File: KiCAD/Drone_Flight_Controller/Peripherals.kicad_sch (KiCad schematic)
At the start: 39 parts, among them J2 Conn_01x03, J3 Conn_01x03, J301 XT60, J302 Conn_01x04, J4 Conn_01x03, J5 Conn_01x03, J6 USB_C_Receptacle_USB2.0_14P, Q501 2N2222A, U3 74AHC1G125, U4 74AHC1G125, U5 74AHC1G125, U6 74AHC1G125

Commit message: Re-annotate
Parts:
- +5V1: renamed from VBUS1; value VBUS -> +5V
- renumbered 3V3 to 3V1, BZ501 to BZ1, C302 to C1, D315 to D1, D4 to D3, D301 to D4, D302 to D5, D3 to D6, D5 to D7, F4 to F3, F3 to F4, J302 to GPS1, J301 to J1, J4 to Motor1, J5 to Motor2, J2 to Motor3, J3 to Motor4, Q501 to Q1, R8 to R1, R1 to R2, R501 to R3, R502 to R4, R303 to R5, R304 to R6, U5 to U1, U6 to U2, J6 to USB-C1

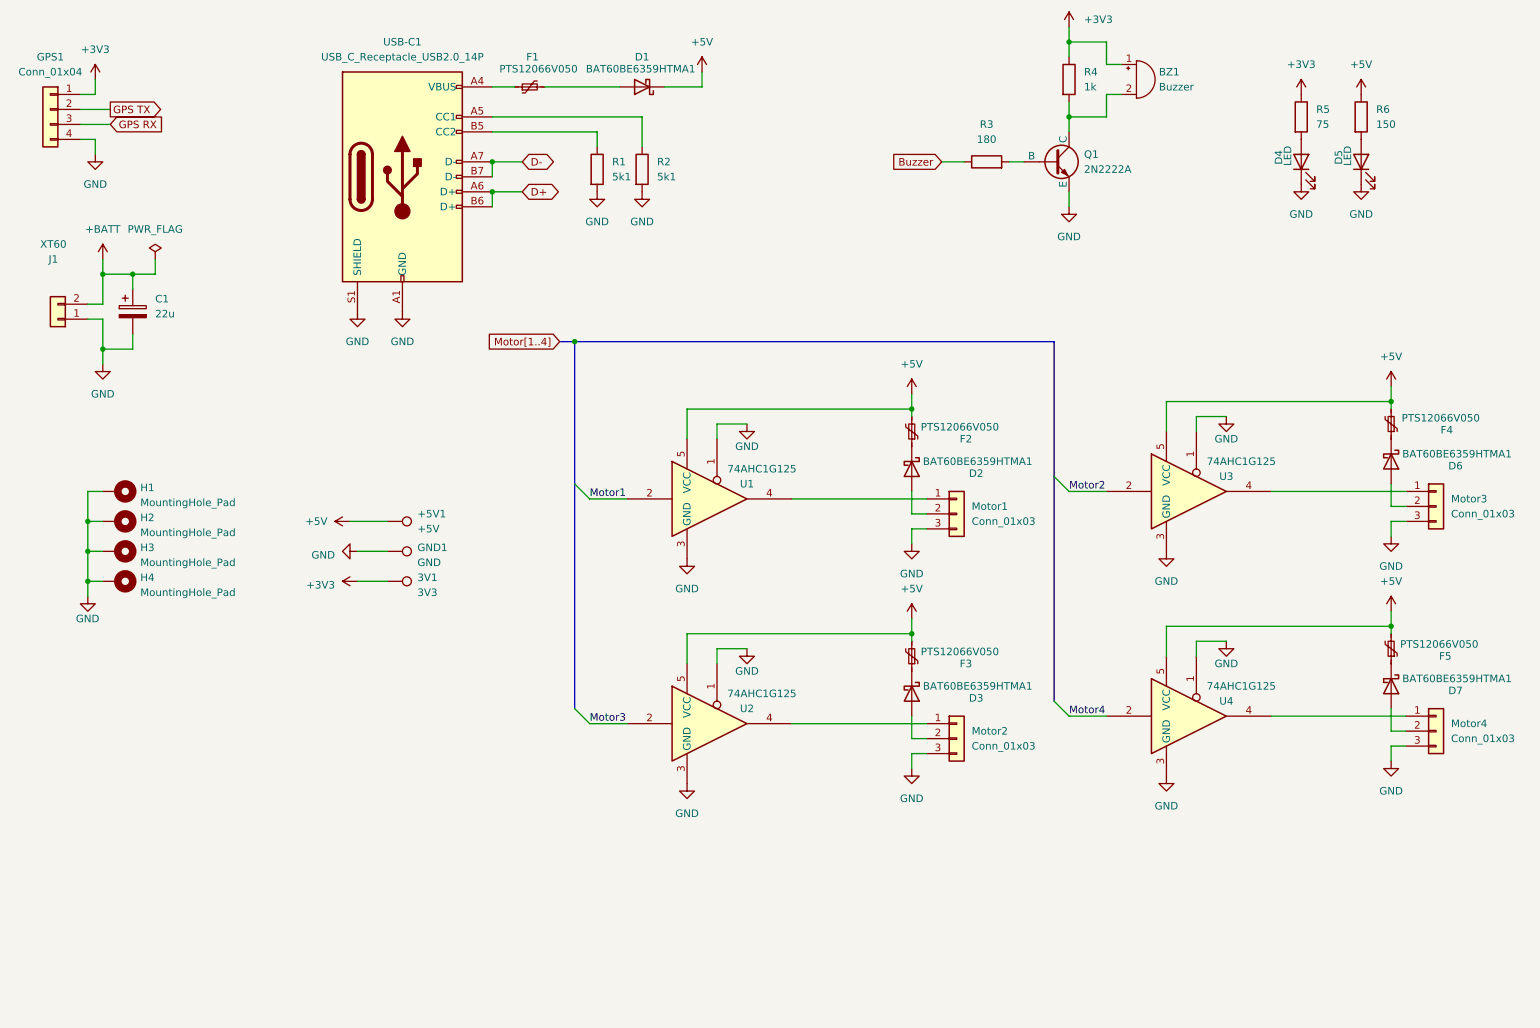
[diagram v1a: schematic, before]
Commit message: Add Status LEDs
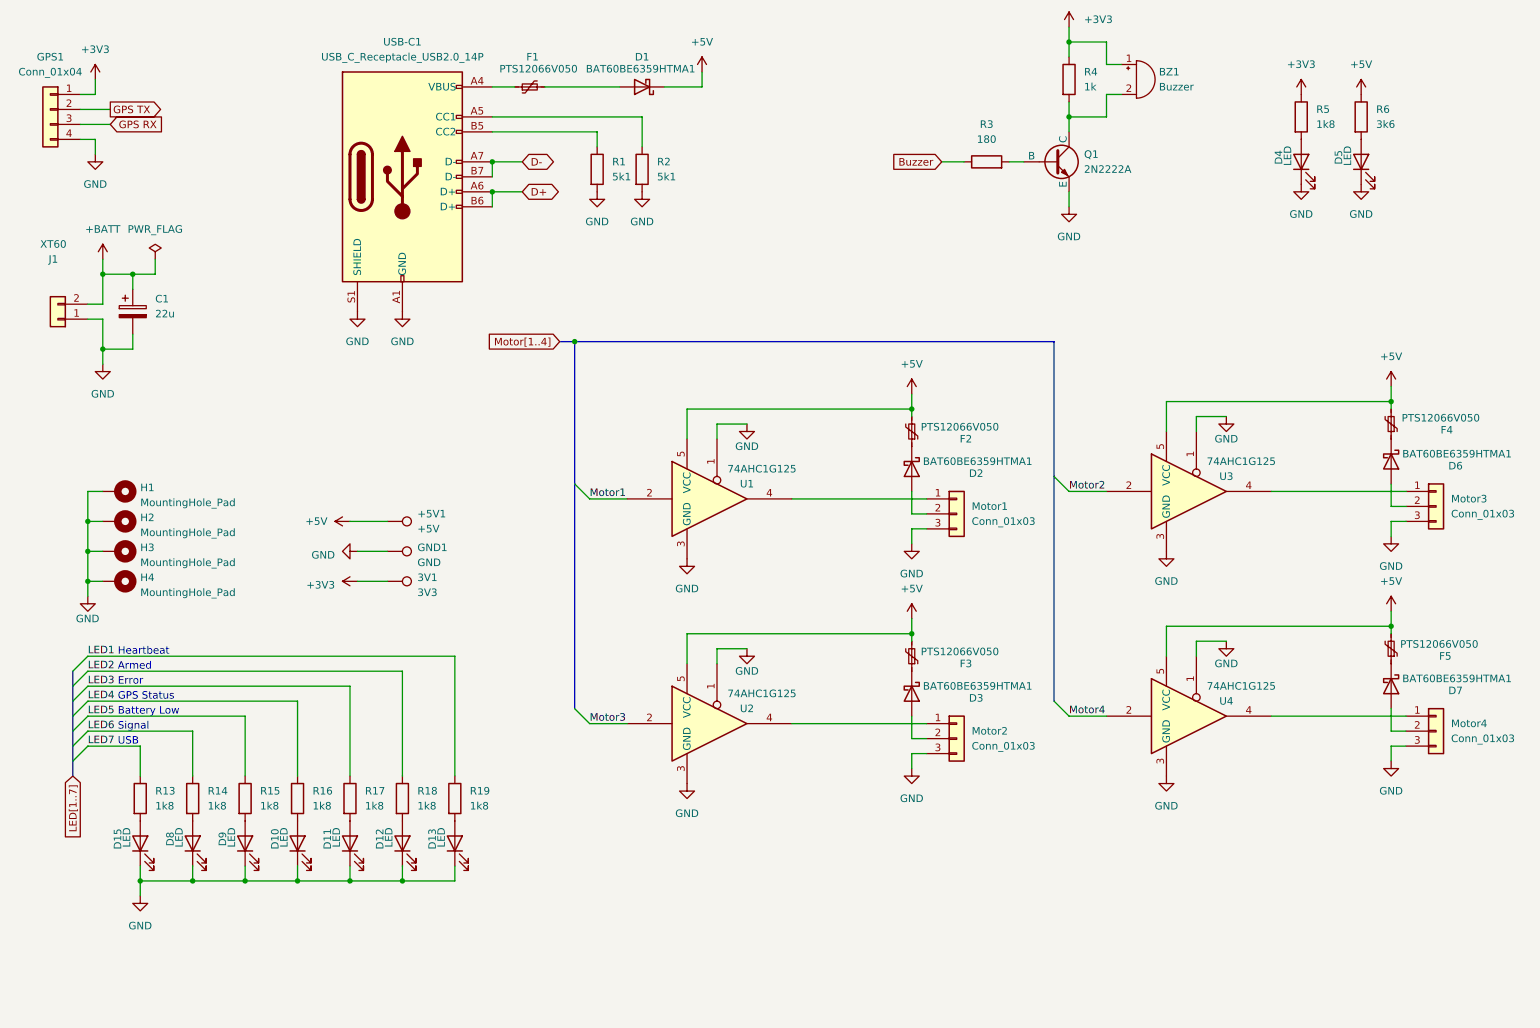
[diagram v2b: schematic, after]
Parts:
- added D10, D11, D12, D13, D15, D8, D9: LED, LED_SMD:LED_0805_2012Metric_Pad1.15x1.40mm_HandSolder, symbol Device:LED
- added R13, R14, R15, R16, R17, R18, R19: 1k8, symbol Device:R
- R5: value 75 -> 1k8; footprint Resistor_SMD:R_0805_2012Metric_Pad1.20x1.40mm_HandSolder -> (none); Link https://eu.mouser.com/ProductDetail/YAGEO/RC0805FR-0775RP?q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 -> (none)
- R6: value 150 -> 3k6
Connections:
- net GND: now also D10.1 (K), D11.1 (K), D12.1 (K), D13.1 (K), D15.1 (K), D8.1 (K), D9.1 (K)
- new net: D12.2 (A), R18.2
- new net: D15.2 (A), R13.2
- new net: D8.2 (A), R14.2
- new net: D11.2 (A), R17.2
- new net: D9.2 (A), R15.2
- new net: D13.2 (A), R19.2
- new net: D10.2 (A), R16.2
- new net LED1: R19.1
- new net LED2: R18.1
- new net LED3: R17.1
- new net LED4: R16.1
- new net LED5: R15.1
- new net LED6: R14.1
- new net LED7: R13.1
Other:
- note added: "Armed"
- note added: "Battery Low"
- note added: "Error"
- note added: "GPS Status"
- note added: "Heartbeat"
- note added: "Signal"
- note added: "USB"

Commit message: Fix Error with Motors
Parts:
- renumbered Motor3 to Motor2, Motor2 to Motor3
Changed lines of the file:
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@@
 		(dnp no)
 		(fields_autoplaced yes)
-		(property "Reference" "Motor3"
+		(property "Reference" "Motor2"
 			(at 269.24 107.9499 0)
 			(effects
@@
 			(project "Drone_Flight_Controller"
 				(path "/51ab9491-7068-4b24-bb38-47a0c739796e/a1832adb-c070-4778-a5ef-97ea378c06da"
-					(reference "Motor3")
+					(reference "Motor2")
 					(unit 1)
 				)
@@
 		(dnp no)
 		(fields_autoplaced yes)
-		(property "Reference" "Motor2"
+		(property "Reference" "Motor3"
 			(at 187.96 147.3199 0)
 			(effects
@@
 			(project "Drone_Flight_Controller"
 				(path "/51ab9491-7068-4b24-bb38-47a0c739796e/a1832adb-c070-4778-a5ef-97ea378c06da"
-					(reference "Motor2")
-					(unit 1)
-				)
+					(reference "Motor3")
+					(unit 1)
+				)

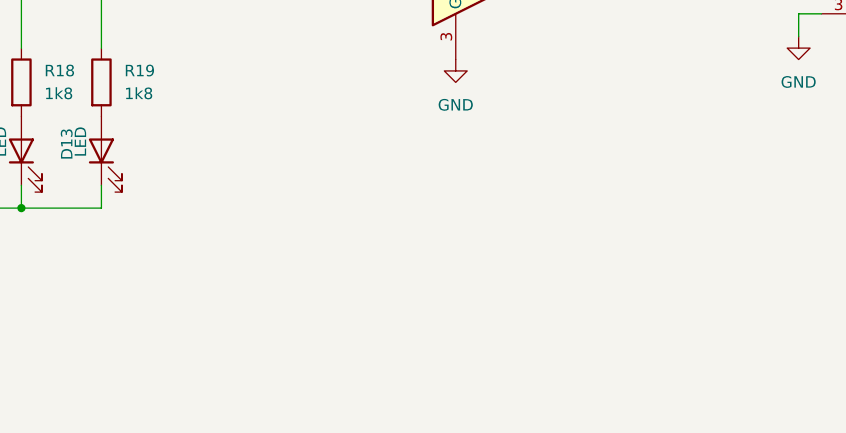
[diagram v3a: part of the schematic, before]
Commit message: Add Current and ESC sense
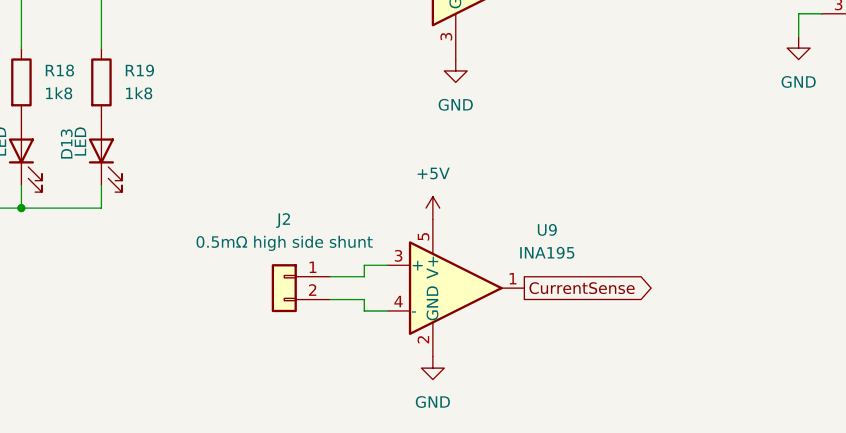
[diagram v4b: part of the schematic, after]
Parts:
- added J2: 0.5mΩ high side shunt, symbol Connector_Generic:Conn_01x02
- added U9: INA195, Package_TO_SOT_SMD:SOT-23-5, symbol Amplifier_Current:INA195
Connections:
- net +5V: now also U9.5 (V+)
- net GND: now also U9.2 (GND)
- new net: J2.1 (Pin_1), U9.3 (+)
- new net: J2.2 (Pin_2), U9.4 (-)
- new net CurrentSense: U9.1

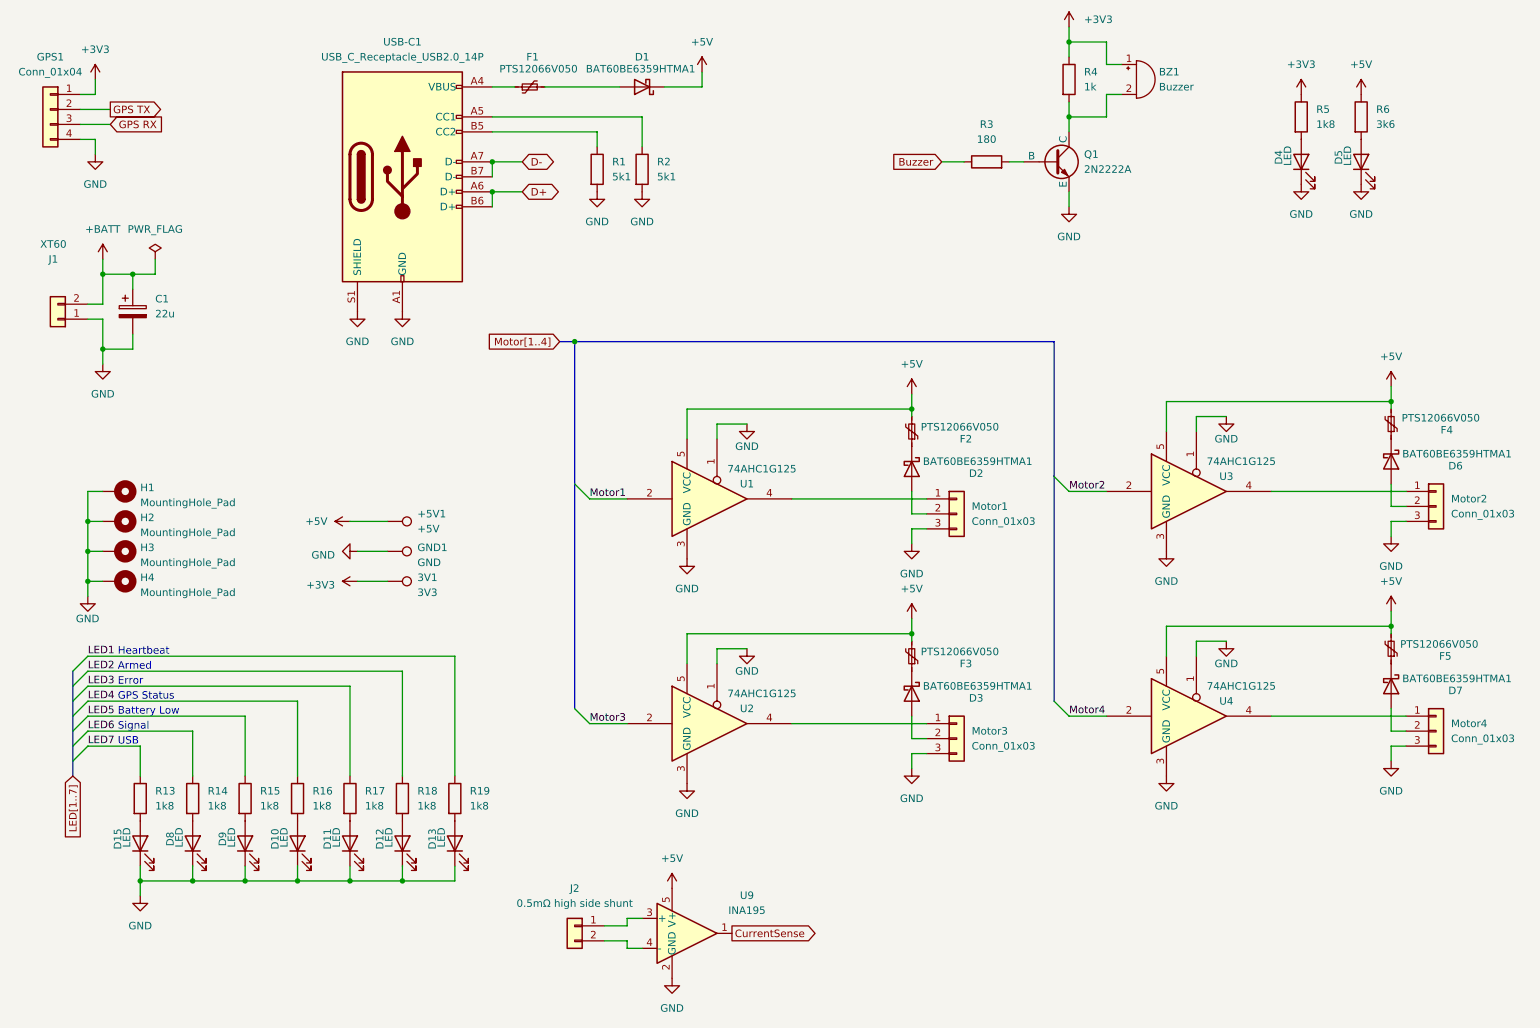
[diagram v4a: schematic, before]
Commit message: Add ESC Sense
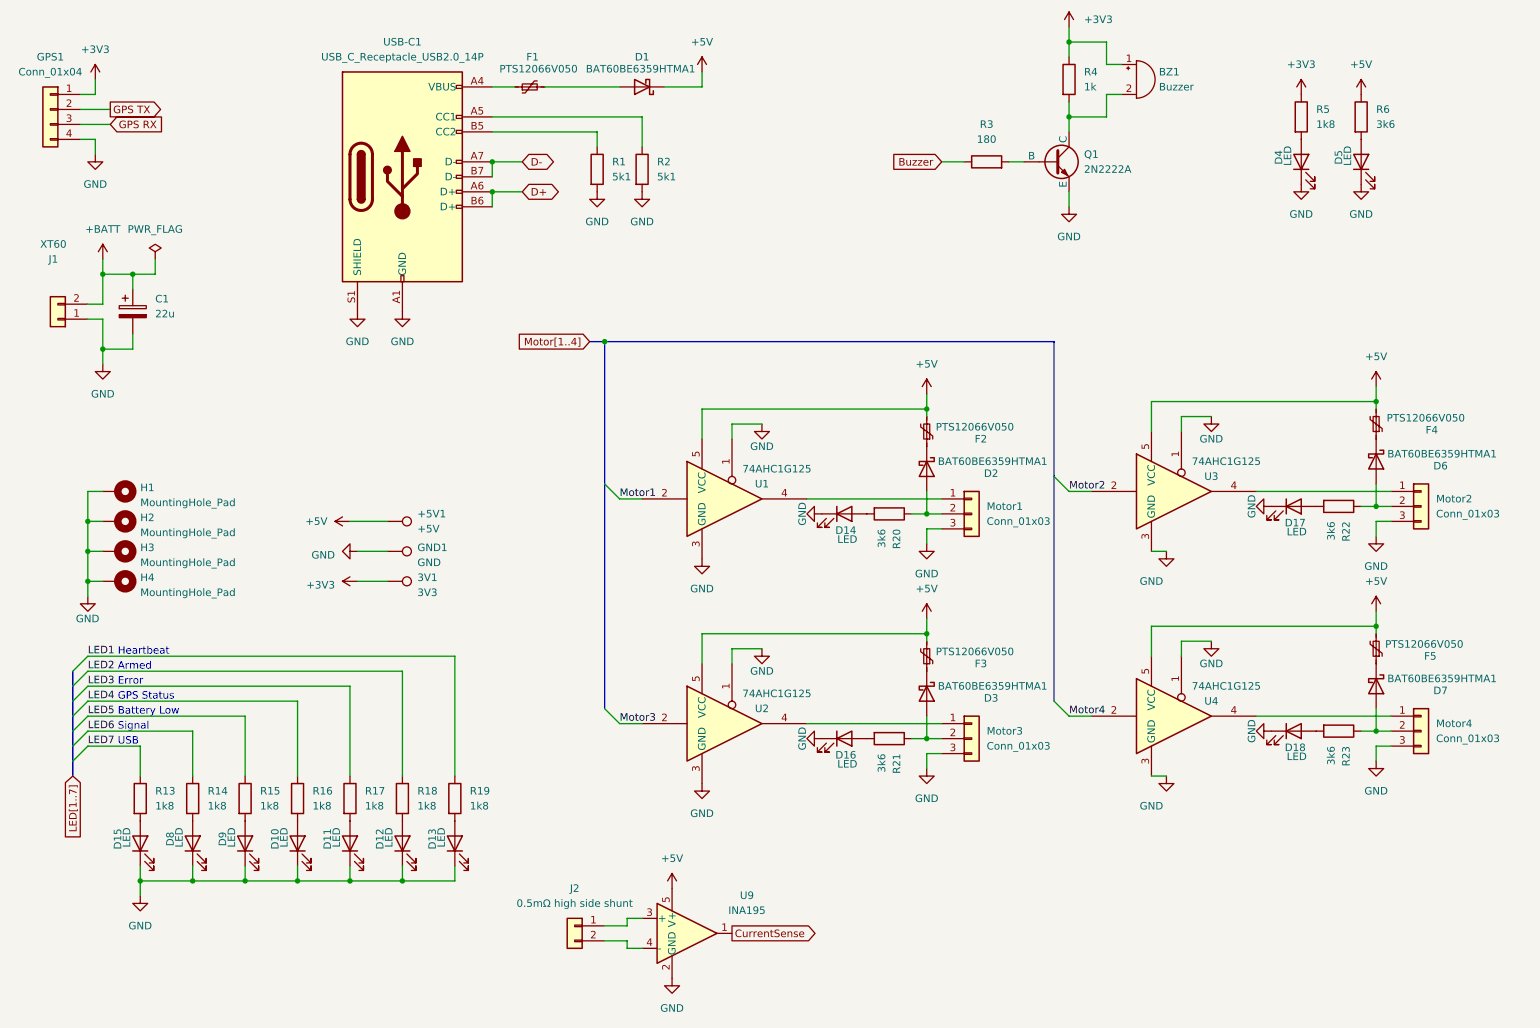
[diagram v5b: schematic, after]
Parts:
- added D14, D16, D17, D18: LED, LED_SMD:LED_0805_2012Metric_Pad1.15x1.40mm_HandSolder, symbol Device:LED
- added R20, R21, R22, R23: 3k6, Resistor_SMD:R_0805_2012Metric_Pad1.20x1.40mm_HandSolder, symbol Device:R
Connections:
- net GND: now also D14.1 (K), D16.1 (K), D17.1 (K), D18.1 (K)
- net at D7.2 (A), Motor4.2 (Pin_2): now also R23.1
- net at D2.2 (A), Motor1.2 (Pin_2): now also R20.1
- net at D6.2 (A), Motor2.2 (Pin_2): now also R22.1
- net at D3.2 (A), Motor3.2 (Pin_2): now also R21.1
- new net: D18.2 (A), R23.2
- new net: D17.2 (A), R22.2
- new net: D14.2 (A), R20.2
- new net: D16.2 (A), R21.2
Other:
- moved on the sheet: D2, D3, D6, D7, F2, F3, F4, F5, Motor1, Motor2, Motor3, Motor4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

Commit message: Add Footprints.
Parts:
- H1, H2, H3, H4: footprint MountingHole:MountingHole_3.2mm_M3_DIN965_Pad -> MountingHole:MountingHole_2.2mm_M2_Pad_TopBottom
- J2: footprint (none) -> Connector_PinHeader_2.54mm:PinHeader_1x02_P2.54mm_Vertical
- R1, R13, R14, R15, R16, R17, R18, R19, R2, R5: footprint (none) -> Resistor_SMD:R_0805_2012Metric_Pad1.20x1.40mm_HandSolder
- USB-C1: footprint (none) -> Connector_USB:USB_C_Receptacle_HRO_TYPE-C-31-M-12
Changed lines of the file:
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@@
 			)
 		)
-		(property "Footprint" "MountingHole:MountingHole_3.2mm_M3_DIN965_Pad"
+		(property "Footprint" "MountingHole:MountingHole_2.2mm_M2_Pad_TopBottom"
 			(at 43.18 106.68 0)
 			(effects
@@
 			)
 		)
-		(property "Footprint" ""
+		(property "Footprint" "Resistor_SMD:R_0805_2012Metric_Pad1.20x1.40mm_HandSolder"
 			(at 242.062 43.18 90)
 			(effects
@@
 			)
 		)
-		(property "Footprint" ""
+		(property "Footprint" "Resistor_SMD:R_0805_2012Metric_Pad1.20x1.40mm_HandSolder"
 			(at 89.662 158.75 90)
 			(effects
@@
 			)
 		)
-		(property "Footprint" "MountingHole:MountingHole_3.2mm_M3_DIN965_Pad"
+		(property "Footprint" "MountingHole:MountingHole_2.2mm_M2_Pad_TopBottom"
 			(at 43.18 111.76 0)
 			(effects
@@
 			)
 		)
-		(property "Footprint" ""
+		(property "Footprint" "Resistor_SMD:R_0805_2012Metric_Pad1.20x1.40mm_HandSolder"
 			(at 130.302 52.07 90)
 			(effects
@@
 			)
 		)
-		(property "Footprint" ""
+		(property "Footprint" "Resistor_SMD:R_0805_2012Metric_Pad1.20x1.40mm_HandSolder"
 			(at 122.682 52.07 90)
 			(effects
@@
 			)
 		)
-		(property "Footprint" ""
+		(property "Footprint" "Resistor_SMD:R_0805_2012Metric_Pad1.20x1.40mm_HandSolder"
 			(at 80.772 158.75 90)
 			(effects
@@
 			)
 		)
-		(property "Footprint" "MountingHole:MountingHole_3.2mm_M3_DIN965_Pad"
+		(property "Footprint" "MountingHole:MountingHole_2.2mm_M2_Pad_TopBottom"
 			(at 43.18 121.92 0)
 			(effects
@@
 			)
 		)
-		(property "Footprint" ""
+		(property "Footprint" "Resistor_SMD:R_0805_2012Metric_Pad1.20x1.40mm_HandSolder"
 			(at 45.212 158.75 90)
 			(effects
@@
 			)
 		)
-		(property "Footprint" ""
+		(property "Footprint" "Resistor_SMD:R_0805_2012Metric_Pad1.20x1.40mm_HandSolder"
 			(at 62.992 158.75 90)
 			(effects
@@
 			)
 		)
-		(property "Footprint" ""
+		(property "Footprint" "Connector_PinHeader_2.54mm:PinHeader_1x02_P2.54mm_Vertical"
 			(at 120.65 180.34 0)
 			(effects
@@
 			)
 		)
-		(property "Footprint" ""
+		(property "Footprint" "Connector_USB:USB_C_Receptacle_HRO_TYPE-C-31-M-12"
 			(at 95.25 53.34 0)
 			(effects
@@
 			)
 		)
-		(property "Footprint" ""
+		(property "Footprint" "Resistor_SMD:R_0805_2012Metric_Pad1.20x1.40mm_HandSolder"
 			(at 71.882 158.75 90)
 			(effects
@@
 			)
 		)
-		(property "Footprint" "MountingHole:MountingHole_3.2mm_M3_DIN965_Pad"
+		(property "Footprint" "MountingHole:MountingHole_2.2mm_M2_Pad_TopBottom"
 			(at 43.18 116.84 0)
 			(effects
@@
 			)
 		)
-		(property "Footprint" ""
+		(property "Footprint" "Resistor_SMD:R_0805_2012Metric_Pad1.20x1.40mm_HandSolder"
 			(at 98.552 158.75 90)
 			(effects
@@
 			)
 		)
-		(property "Footprint" ""
+		(property "Footprint" "Resistor_SMD:R_0805_2012Metric_Pad1.20x1.40mm_HandSolder"
 			(at 54.102 158.75 90)
 			(effects
